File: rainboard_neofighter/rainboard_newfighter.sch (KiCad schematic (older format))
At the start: 95 parts, among them J1 Conn_01x02, J10 Conn_01x03, J11 SDS-50J, J12 SDS-50J, J13 Conn_01x02, J14 Conn_01x02, J15 Conn_01x02, J16 Conn_01x02, J17 Conn_01x02, J18 Conn_01x02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

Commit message: v0.2 complete and send to fab
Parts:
- added R10, R9: 4.7k, Resistor_SMD:R_0603_1608Metric, symbol Device:R
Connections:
- net 5V: now also R10.1, R9.1
- net SCL: now also R9.2
- net SDA: now also R10.2
- net softpot-1: now also XA1.A10; no longer XA1.A9
- net softpot-2: now also XA1.A9; no longer XA1.A10

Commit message: V0.2 complete and sent to manufacture
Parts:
- added D?: D, Diode_SMD:D_SMA, symbol Device:D
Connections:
- net softpot-1: no longer XA1.A10
- net softpot-2: now also XA1.A10
- net at R7.2, U3.1: now also D?.1 (K)
- net at J11.5, U3.2: now also D?.2 (A)
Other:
- moved on the sheet: R8, U3
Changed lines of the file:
@@
 Text GLabel 1050 3250 0    50   Input ~ 0
 softpot-2
-Text GLabel 1050 3350 0    50   Input ~ 0
-softpot-1
 Wire Wire Line
 	1050 3250 1650 3250
@@
 L opto_couplers:EL357N(A)(TA)-G U3
 U 1 1 607274ED
-P 15050 12000
-F 0 "U3" V 15004 12233 50  0000 L CNN
-F 1 "EL357N(A)(TA)-G" V 15095 12233 50  0000 L CNN
-F 2 "opto_coupler:SOP254P700X200-4N" H 15050 12000 50  0001 L BNN
-F 3 "IPC-7351B" H 15050 12000 50  0001 L BNN
-F 4 "EL357N_A__TA_-G" H 15050 12000 50  0001 L BNN "Field4"
-F 5 "0.10 USD" H 15050 12000 50  0001 L BNN "Field5"
-F 6 "SOP-4 Everlight" H 15050 12000 50  0001 L BNN "Field6"
-F 7 "Good" H 15050 12000 50  0001 L BNN "Field7"
-F 8 "Everlight" H 15050 12000 50  0001 L BNN "Field8"
-F 9 "Optocoupler [Everlight Electronics] EL357N_A__TA_-G Optocoupler" H 15050 12000 50  0001 L BNN "Field9"
-F 10 "C142286" V 15050 12000 50  0001 C CNN "LCSC"
-	1    15050 12000
+P 15300 12000
+F 0 "U3" V 15254 12233 50  0000 L CNN
+F 1 "EL357N(A)(TA)-G" V 15345 12233 50  0000 L CNN
+F 2 "opto_coupler:SOP254P700X200-4N" H 15300 12000 50  0001 L BNN
+F 3 "IPC-7351B" H 15300 12000 50  0001 L BNN
+F 4 "EL357N_A__TA_-G" H 15300 12000 50  0001 L BNN "Field4"
+F 5 "0.10 USD" H 15300 12000 50  0001 L BNN "Field5"
+F 6 "SOP-4 Everlight" H 15300 12000 50  0001 L BNN "Field6"
+F 7 "Good" H 15300 12000 50  0001 L BNN "Field7"
+F 8 "Everlight" H 15300 12000 50  0001 L BNN "Field8"
+F 9 "Optocoupler [Everlight Electronics] EL357N_A__TA_-G Optocoupler" H 15300 12000 50  0001 L BNN "Field9"
+F 10 "C142286" V 15300 12000 50  0001 C CNN "LCSC"
+	1    15300 12000
 	1    0    0    -1
 $EndComp
@@
 	14100 11800 14200 11800
 Wire Wire Line
-	14200 11800 14200 12100
-Wire Wire Line
-	14200 12100 14550 12100
-Wire Wire Line
-	15750 11300 15750 11400
+	16000 11300 16000 11400
 $Comp
 L Device:R R8
 U 1 1 61396682
-P 15750 11550
-F 0 "R8" H 15680 11504 50  0000 R CNN
-F 1 "10k" H 15680 11595 50  0000 R CNN
-F 2 "Resistor_SMD:R_0603_1608Metric" V 15680 11550 50  0001 C CNN
-F 3 "~" H 15750 11550 50  0001 C CNN
-F 4 "C25804" H 15750 11550 50  0001 C CNN "LCSC"
-	1    15750 11550
+P 16000 11550
+F 0 "R8" H 15930 11504 50  0000 R CNN
+F 1 "10k" H 15930 11595 50  0000 R CNN
+F 2 "Resistor_SMD:R_0603_1608Metric" V 15930 11550 50  0001 C CNN
+F 3 "~" H 16000 11550 50  0001 C CNN
+F 4 "C25804" H 16000 11550 50  0001 C CNN "LCSC"
+	1    16000 11550
 	-1   0    0    1
 $EndComp
-Text GLabel 15750 11300 2    50   Input ~ 0
+Text GLabel 16000 11300 2    50   Input ~ 0
 5V
 $Comp
 L power:Earth #PWR0109
 U 1 1 60777E72
-P 15550 12100
-F 0 "#PWR0109" H 15550 11850 50  0001 C CNN
-F 1 "Earth" H 15550 11950 50  0001 C CNN
-F 2 "" H 15550 12100 50  0001 C CNN
-F 3 "~" H 15550 12100 50  0001 C CNN
-	1    15550 12100
+P 15800 12100
+F 0 "#PWR0109" H 15800 11850 50  0001 C CNN
+F 1 "Earth" H 15800 11950 50  0001 C CNN
+F 2 "" H 15800 12100 50  0001 C CNN
+F 3 "~" H 15800 12100 50  0001 C CNN
+	1    15800 12100
 	1    0    0    -1
 $EndComp
@@
 MIDI-IN
 Wire Wire Line
-	15750 11700 15750 11800
-Wire Wire Line
-	15750 11900 15550 11900
-Connection ~ 15750 11800
-Wire Wire Line
-	15750 11800 15750 11900
+	16000 11700 16000 11800
+Wire Wire Line
+	16000 11900 15800 11900
+Connection ~ 16000 11800
+Wire Wire Line
+	16000 11800 16000 11900
 Text GLabel 1250 1250 0    50   Input ~ 0
 MIDI-IN
@@
 	17400 12650 18550 12650
 Wire Wire Line
-	15750 11800 17400 11800
+	16000 11800 17400 11800
 Wire Wire Line
 	19950 12550 20050 12550
@@
 Wire Wire Line
 	2900 10350 2950 10350
+Text GLabel 1050 3350 0    50   Input ~ 0
+softpot-2
+$Comp
+L Device:D D?
+U 1 1 5F7937EC
+P 14650 12050
+F 0 "D?" V 14604 12129 50  0000 L CNN
+F 1 "D" V 14695 12129 50  0000 L CNN
+F 2 "Diode_SMD:D_SMA" H 14650 12050 50  0001 C CNN
+F 3 "~" H 14650 12050 50  0001 C CNN
+F 4 "C95872" V 14650 12050 50  0001 C CNN "LCSC"
+	1    14650 12050
+	0    1    1    0
+$EndComp
+Wire Wire Line
+	14800 11900 14650 11900
+Connection ~ 14650 11900
+Wire Wire Line
+	14650 11900 14550 11900
+Wire Wire Line
+	14800 12100 14800 12200
+Wire Wire Line
+	14800 12200 14650 12200
+Wire Wire Line
+	14200 11800 14200 12200
+Connection ~ 14650 12200
+Wire Wire Line
+	14650 12200 14200 12200
 $EndSCHEMATC

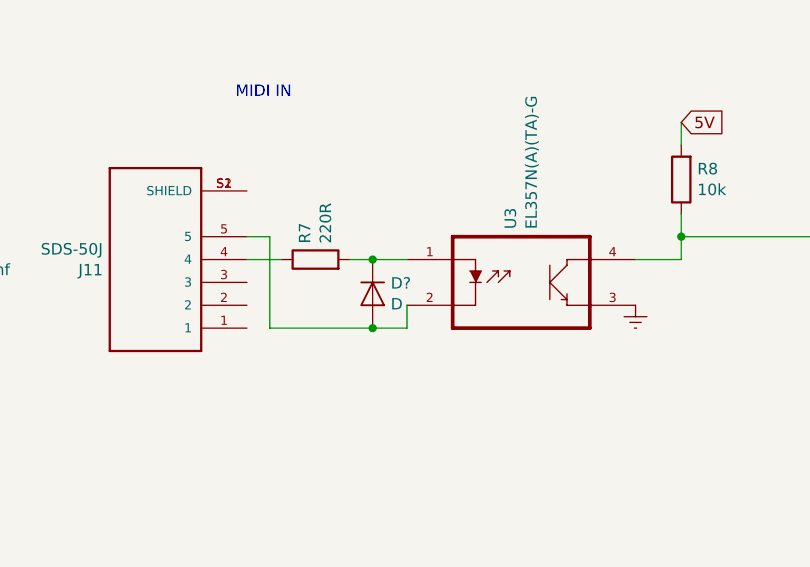
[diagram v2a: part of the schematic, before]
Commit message: check in solver for PCB shape
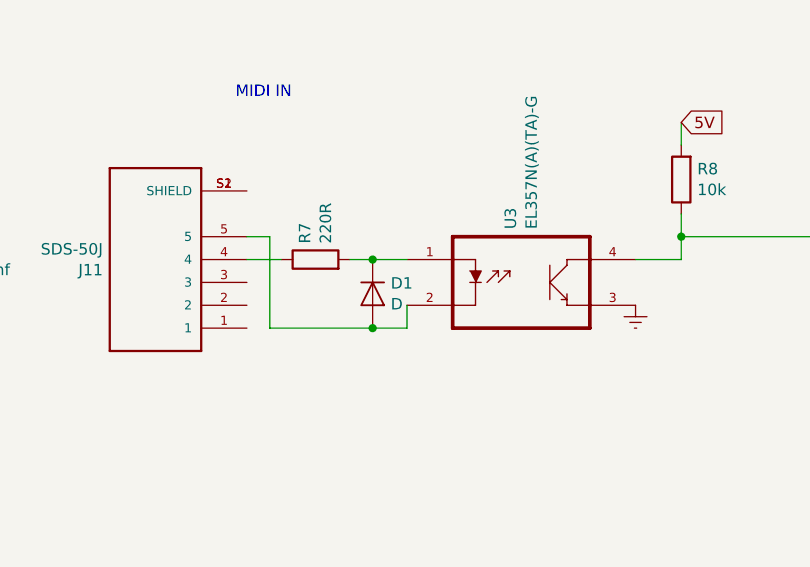
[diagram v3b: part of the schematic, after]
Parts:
- gave numbers to parts that had none: 1
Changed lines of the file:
@@
 softpot-2
 $Comp
-L Device:D D?
+L Device:D D1
 U 1 1 5F7937EC
 P 14650 12050
-F 0 "D?" V 14604 12129 50  0000 L CNN
+F 0 "D1" V 14604 12129 50  0000 L CNN
 F 1 "D" V 14695 12129 50  0000 L CNN
 F 2 "Diode_SMD:D_SMA" H 14650 12050 50  0001 C CNN

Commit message: PCB v0.3
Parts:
- R5, R6, R7: LCSC C4190 -> C22962
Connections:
- net Earth: no longer J12.1, J12.3
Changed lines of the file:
@@
 F 2 "Resistor_SMD:R_0603_1608Metric" V 20030 11200 50  0001 C CNN
 F 3 "~" H 20100 11200 50  0001 C CNN
-F 4 "C4190" H 20100 11200 50  0001 C CNN "LCSC"
+F 4 "C22962" H 20100 11200 50  0001 C CNN "LCSC"
 	1    20100 11200
 	1    0    0    -1
@@
 F 2 "Resistor_SMD:R_0603_1608Metric" V 20080 12200 50  0001 C CNN
 F 3 "~" H 20150 12200 50  0001 C CNN
-F 4 "C4190" H 20150 12200 50  0001 C CNN "LCSC"
+F 4 "C22962" H 20150 12200 50  0001 C CNN "LCSC"
 	1    20150 12200
 	1    0    0    -1
@@
 F 2 "Resistor_SMD:R_0603_1608Metric" V 14330 11900 50  0001 C CNN
 F 3 "~" H 14400 11900 50  0001 C CNN
-F 4 "C4190" H 14400 11900 50  0001 C CNN "LCSC"
+F 4 "C22962" H 14400 11900 50  0001 C CNN "LCSC"
 	1    14400 11900
 	0    -1   -1   0
@@
 Wire Wire Line
 	18550 12950 18550 12850
-Wire Wire Line
-	20800 11750 20800 11650
-Connection ~ 20800 11650
-Wire Wire Line
-	20800 11650 20800 11550
 $Comp
 L Connector_Generic:Conn_01x03 J9
